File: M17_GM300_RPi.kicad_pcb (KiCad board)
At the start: 2 copper layers, 85 x 56 mm, 49 parts, among them J1 RJ45, J2 SJ1-3523N, J3 1935161, J4 DB9_Female, J5 RPi Header, Q1 2N7000, Q2 2N7000, Q3 2N7000, Q4 2N7000, U1 LM2576HVS-5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

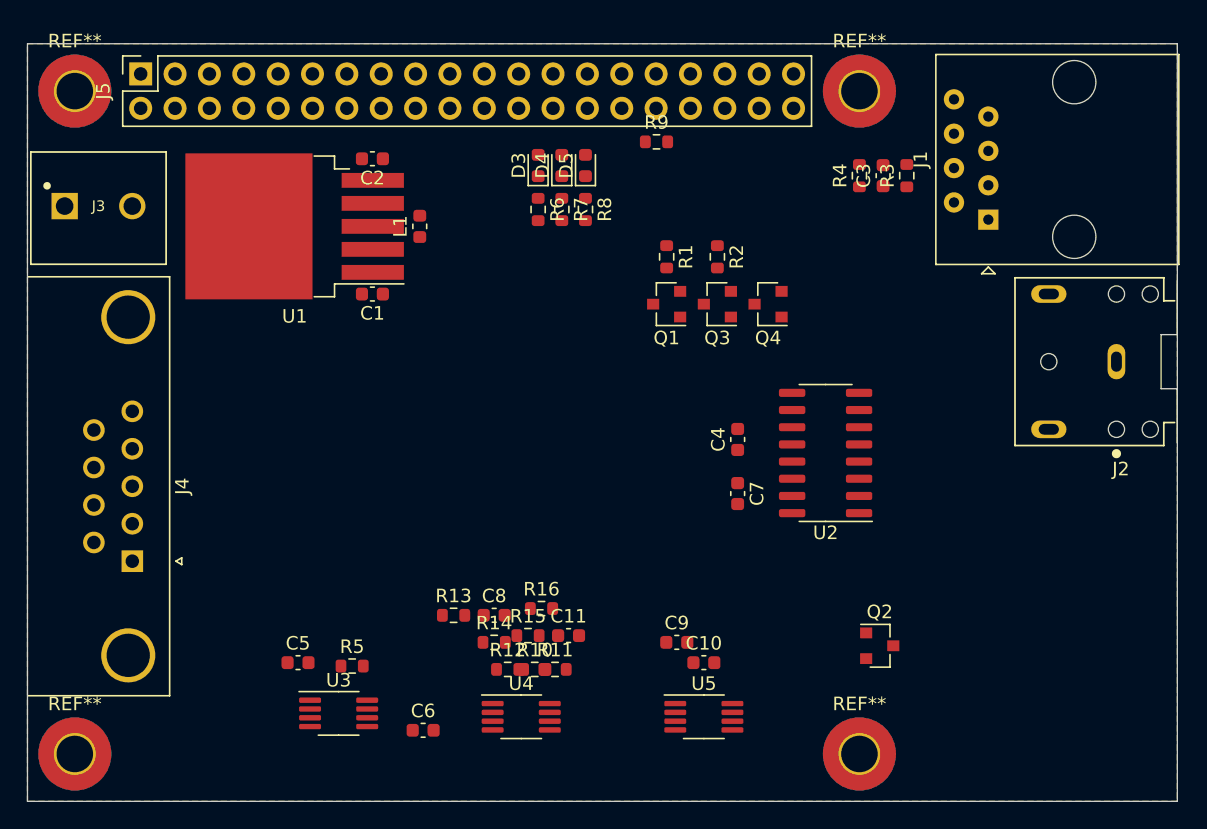
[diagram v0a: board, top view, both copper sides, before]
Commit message: pcb parts grouped by function
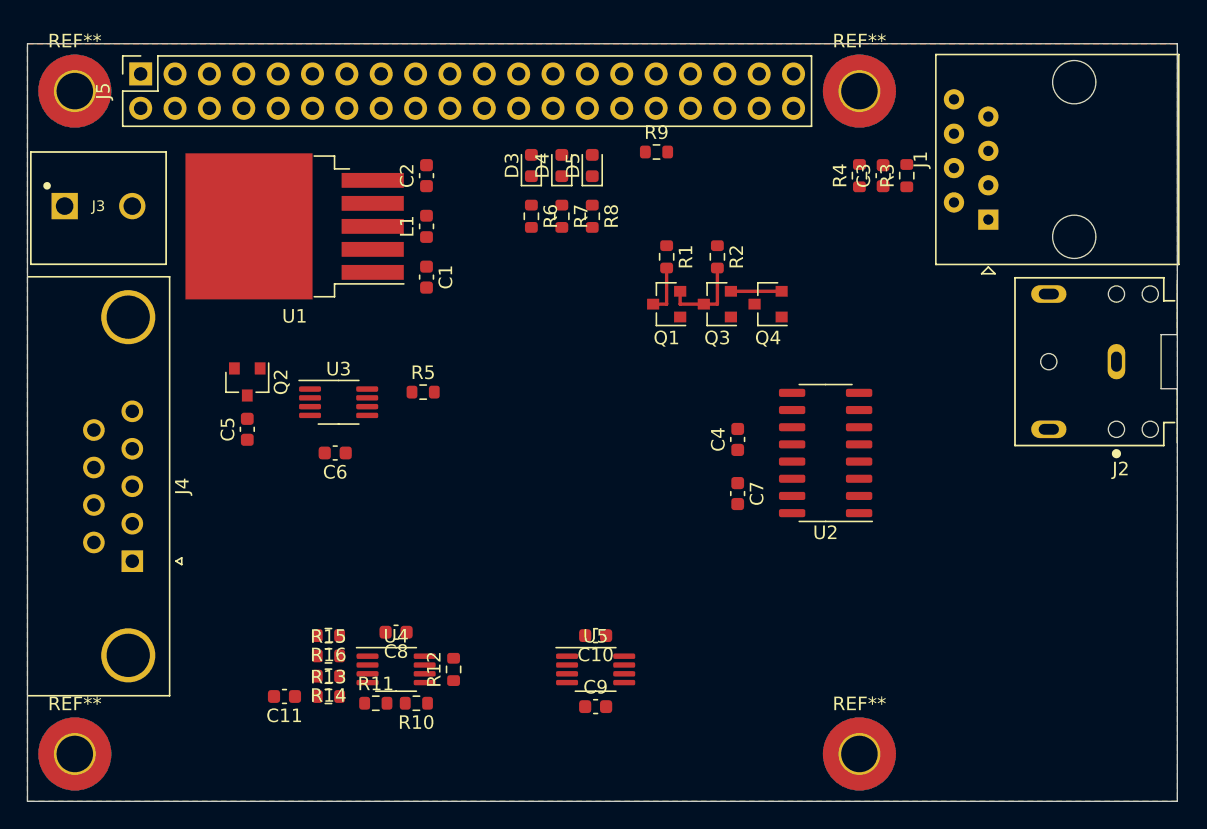
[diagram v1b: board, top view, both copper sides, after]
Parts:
- moved Q2 50.7 mm to (181.2, 75.0), turned to 270 degrees
- moved U3 23.0 mm to (188.0, 76.5)
- moved C6 21.5 mm to (187.8, 80.2), turned to 180 degrees
- moved C11 21.5 mm to (184.0, 98.2), turned to 180 degrees
- moved R5 20.9 mm to (194.2, 75.8)
- moved C5 17.7 mm to (181.2, 78.5), turned to 90 degrees
- moved R16 15.9 mm to (187.2, 93.8), turned to 180 degrees
- moved R15 14.8 mm to (187.2, 95.2)
- moved R11 13.5 mm to (190.8, 98.8)
- moved R14 12.5 mm to (187.2, 96.8), turned to 180 degrees
- moved R13 11.0 mm to (187.2, 98.2)
- moved U4 9.89 mm to (192.2, 96.2)
- moved R10 9.10 mm to (193.8, 98.8), turned to 180 degrees
- moved U5 8.73 mm to (207.0, 96.2)
- moved C10 8.25 mm to (207.0, 93.8), turned to 180 degrees
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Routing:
- net SW2: track 0.00 -> 6.38 mm
- net TX_EN: track 0.00 -> 3.75 mm
- net SW1: track 0.00 -> 3.67 mm

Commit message: Created new symbol and footprint for new power supply; removed old and added new power supply to schem; updated pcb with the changes.
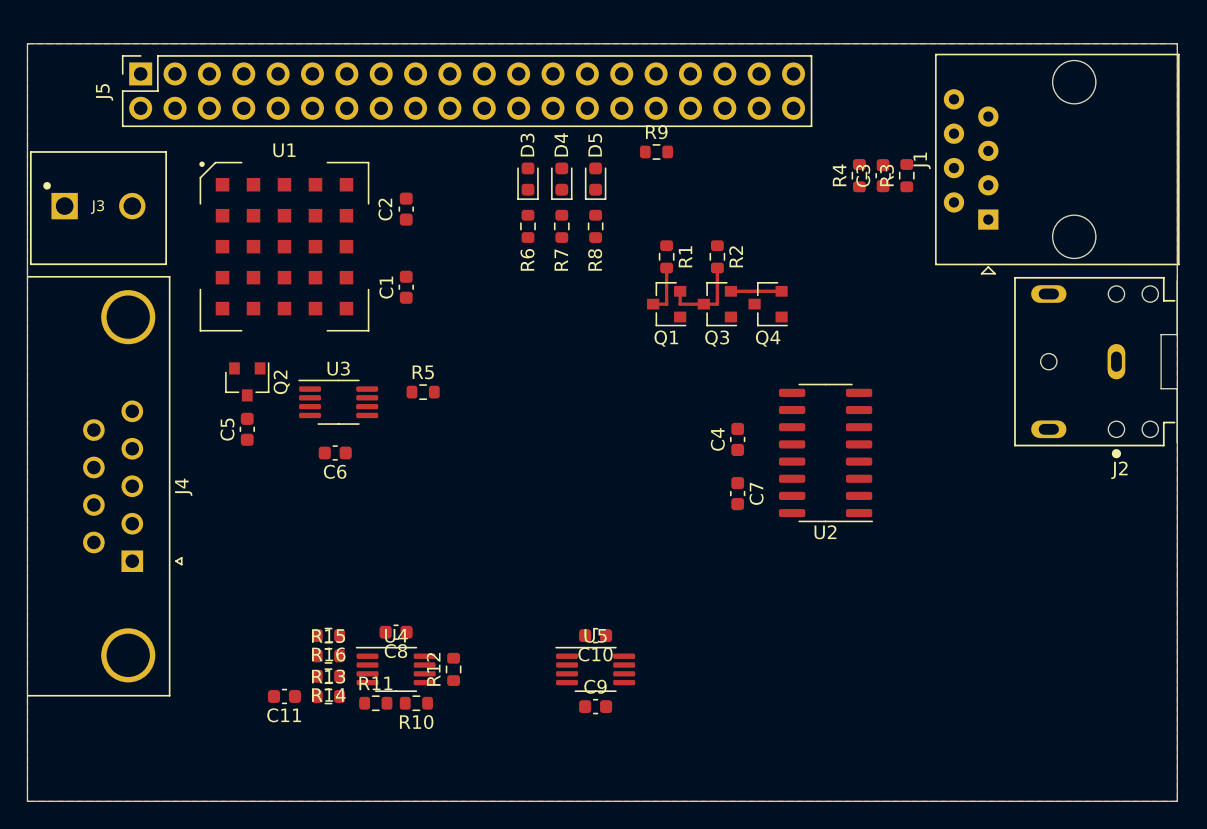
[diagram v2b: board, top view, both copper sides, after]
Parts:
- removed L1: 100 uH, Inductor_SMD:L_0603_1608Metric
- removed REF** (x4): MountingHole_2.7mm_M2.5_Pad_TopBottom, MountingHole:MountingHole_2.7mm_M2.5_Pad_TopBottom
- C1: value 100 uF -> 1000 uF
- U1: value LM2576HVS-5 -> RPM5.0-6.0; footprint Package_TO_SOT_SMD:TO-263-5_TabPin3 -> Power_Supplies:RPM5.0-6.0
- moved C2 2.89 mm to (193.0, 62.2), turned to 270 degrees
- moved C1 1.68 mm to (193.0, 68.0), turned to 90 degrees
- moved U1 1.68 mm to (184.0, 65.0), turned to 0 degrees
- moved D3 1.03 mm to (202.0, 60.0)
- moved D5 1.03 mm to (207.0, 60.0)
- moved D4 1.00 mm to (204.5, 60.0)
- moved R6 0.79 mm to (202.0, 63.5)
- moved R8 0.79 mm to (207.0, 63.5)
- moved R7 0.75 mm to (204.5, 63.5)

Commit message: increased passives to 0805. preliminary layout.
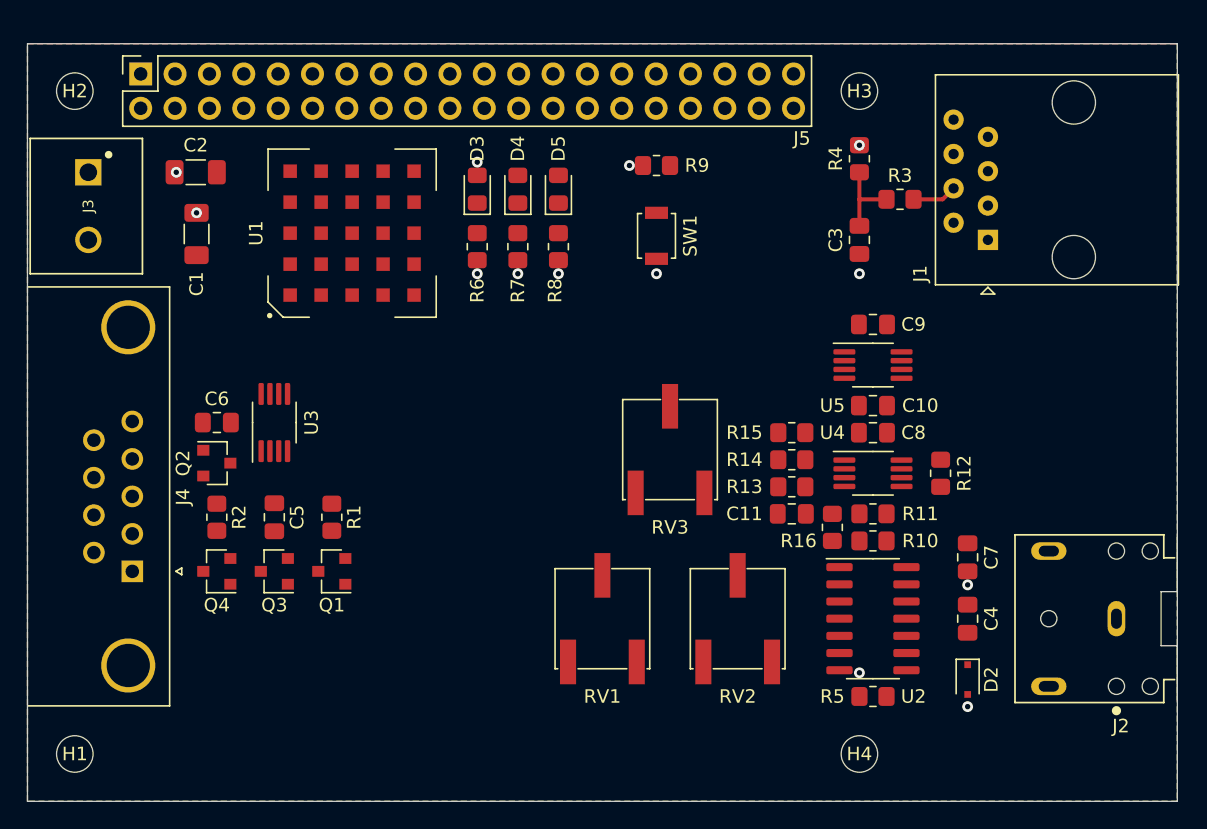
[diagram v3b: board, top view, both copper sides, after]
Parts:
- added D2: 2V7, Diode_SMD:D_SOD-323F, F.Cu at (234.5, 97.0)
- added H1: MountingHole, MountingHole:MountingHole_2.7mm_M2.5, F.Cu at (168.5, 102.5)
- added H2: MountingHole, MountingHole:MountingHole_2.7mm_M2.5, F.Cu at (168.5, 53.5)
- added H3: MountingHole, MountingHole:MountingHole_2.7mm_M2.5, F.Cu at (226.5, 53.5)
- added H4: MountingHole, MountingHole:MountingHole_2.7mm_M2.5, F.Cu at (226.5, 102.5)
- added RV1: 1K, Potentiometer_SMD:Potentiometer_Bourns_3361P_Vertical, F.Cu at (207.5, 92.5)
- added RV2: 4K7, Potentiometer_SMD:Potentiometer_Bourns_3361P_Vertical, F.Cu at (217.5, 92.5)
- added RV3: 4K7, Potentiometer_SMD:Potentiometer_Bourns_3361P_Vertical, F.Cu at (212.5, 80.0)
- added SW1: SW_Push, Button_Switch_SMD:SW_SPST_B3U-1000P, F.Cu at (211.5, 64.2)
- C1, C2: footprint Capacitor_SMD:C_0603_1608Metric -> Capacitor_SMD:C_1206_3216Metric_Pad1.33x1.80mm_HandSolder
- C10, C11, C3, C4, C5, C6, C7, C8, C9: footprint Capacitor_SMD:C_0603_1608Metric -> Capacitor_SMD:C_0805_2012Metric_Pad1.18x1.45mm_HandSolder
- D3, D4, D5: footprint LED_SMD:LED_0603_1608Metric -> LED_SMD:LED_0805_2012Metric_Pad1.15x1.40mm_HandSolder
- R1, R10, R11, R12, R13, R14, R15, R16, R2, R3, R4, R5, R6, R7, R8, R9: footprint Resistor_SMD:R_0603_1608Metric -> Resistor_SMD:R_0805_2012Metric_Pad1.20x1.40mm_HandSolder
- U2: footprint Package_SO:SOIC-16_3.9x9.9mm_P1.27mm -> Package_SO:SOIC-14_3.9x8.7mm_P1.27mm
- moved Q4 45.3 mm to (179.0, 89.0)
- moved R2 41.7 mm to (179.0, 85.0)
- moved R5 40.1 mm to (227.5, 98.2)
- moved C11 39.9 mm to (221.5, 84.8)
- moved R11 39.3 mm to (227.5, 84.8)
- moved R12 38.8 mm to (232.5, 81.8)
- moved Q3 38.2 mm to (183.2, 89.0)
- moved C8 38.2 mm to (227.5, 78.8)
- moved U4 38.1 mm to (227.5, 81.8)
- moved R16 38.1 mm to (224.5, 85.8), turned to 270 degrees
- moved R15 38.0 mm to (221.5, 78.8)
- moved R14 37.8 mm to (221.5, 80.8)
- moved R13 37.6 mm to (221.5, 82.8)
- moved R10 35.8 mm to (227.5, 86.8), turned to 0 degrees
- moved C9 34.9 mm to (227.5, 70.8), turned to 180 degrees
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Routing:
- net SW2: track 6.38 -> 0.00 mm
- net Net-(C3-Pad1): track 0.00 -> 5.96 mm
- net TX_EN: track 3.75 -> 0.00 mm
- net SW1: track 3.67 -> 0.00 mm
- net MIC: track 0.00 -> 3.30 mm
- net GND: vias 0 -> 10
- net +BATT: vias 0 -> 1
- net +5V: vias 0 -> 1
- net +3V3: vias 0 -> 1
- added copper zone on PWR, net +3V3
- added copper zone on B.Cu, net GND
- added copper zone on GND, net GND
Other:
- copper layers 2 -> 4

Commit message: updated layout to proposed final
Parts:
- U3: footprint Package_SO:MSOP-8_3x3mm_P0.65mm -> Package_SO:SOIC-8_3.9x4.9mm_P1.27mm
- moved C6 30.6 mm to (209.0, 84.0), turned to 90 degrees
- moved R5 30.1 mm to (201.0, 84.0), turned to 270 degrees
- moved U3 24.8 mm to (205.0, 90.0), turned to 0 degrees
- moved C5 21.8 mm to (205.0, 84.0)
- moved RV3 20.3 mm to (216.0, 100.0)
- moved C9 17.0 mm to (241.0, 81.0)
- moved RV1 15.4 mm to (194.0, 100.0)
- moved RV2 14.6 mm to (205.0, 100.0)
- moved C10 14.0 mm to (241.0, 73.0)
- moved C11 13.9 mm to (229.0, 73.0), turned to 0 degrees
- moved U5 13.9 mm to (241.0, 77.0)
- moved R11 10.8 mm to (235.0, 77.0)
- moved R13 9.86 mm to (223.0, 73.0)
- moved R10 9.45 mm to (235.0, 81.0), turned to 180 degrees
- moved R1 9.18 mm to (183.0, 77.0)
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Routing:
- net Net-(C4-Pad1): track 0.00 -> 11.4 mm
- net Net-(C3-Pad1): track 5.96 -> 0.00 mm, vias 0 -> 1
- net MIC: track 3.30 -> 0.00 mm
- net GND: vias 10 -> 9
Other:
- board text added: "GM300 to RPi Interface Board"
- board text added: "RX Gain"
- board text added: "RX Vol"
- board text added: "TX Dev"
- board text added: "prototype"

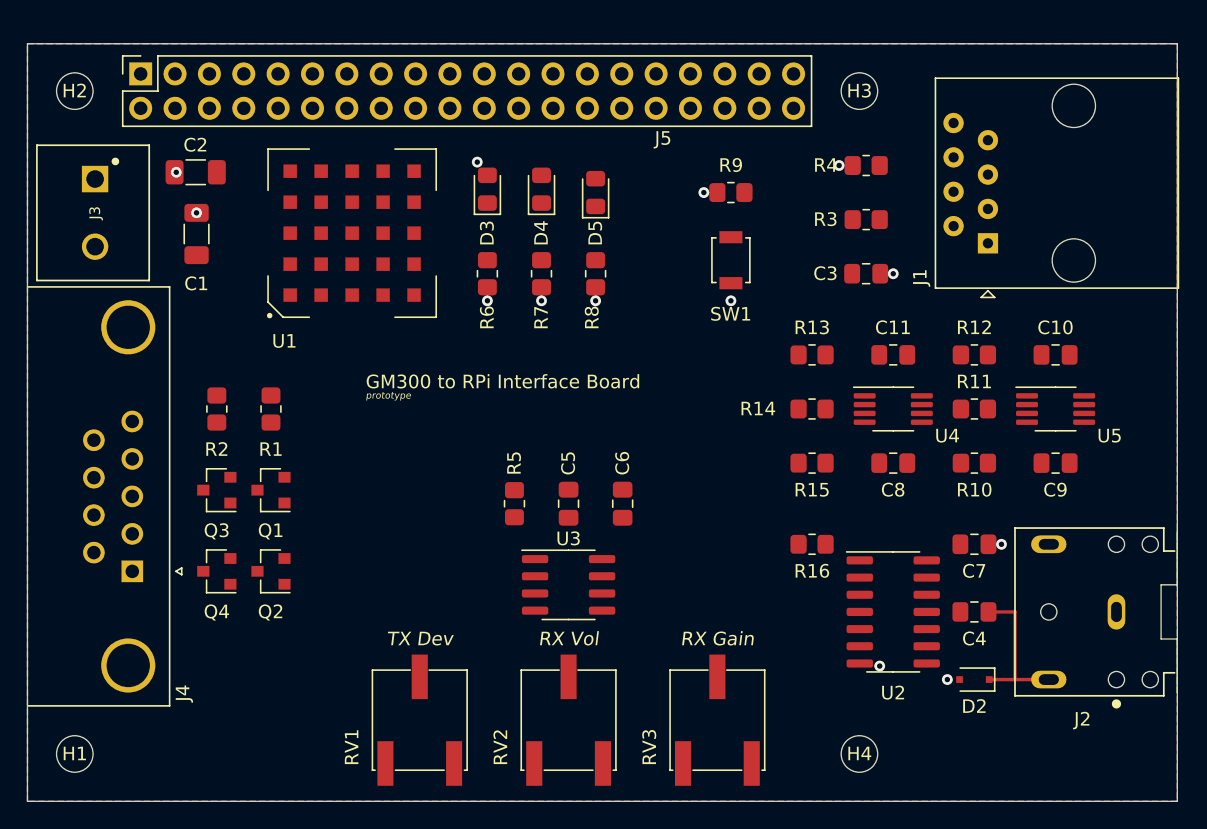
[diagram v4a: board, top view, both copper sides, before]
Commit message: part and footprint updates, routing
updated parts and footprints for header and transistors. updated layout. most routing is complete pending changes to schematic.
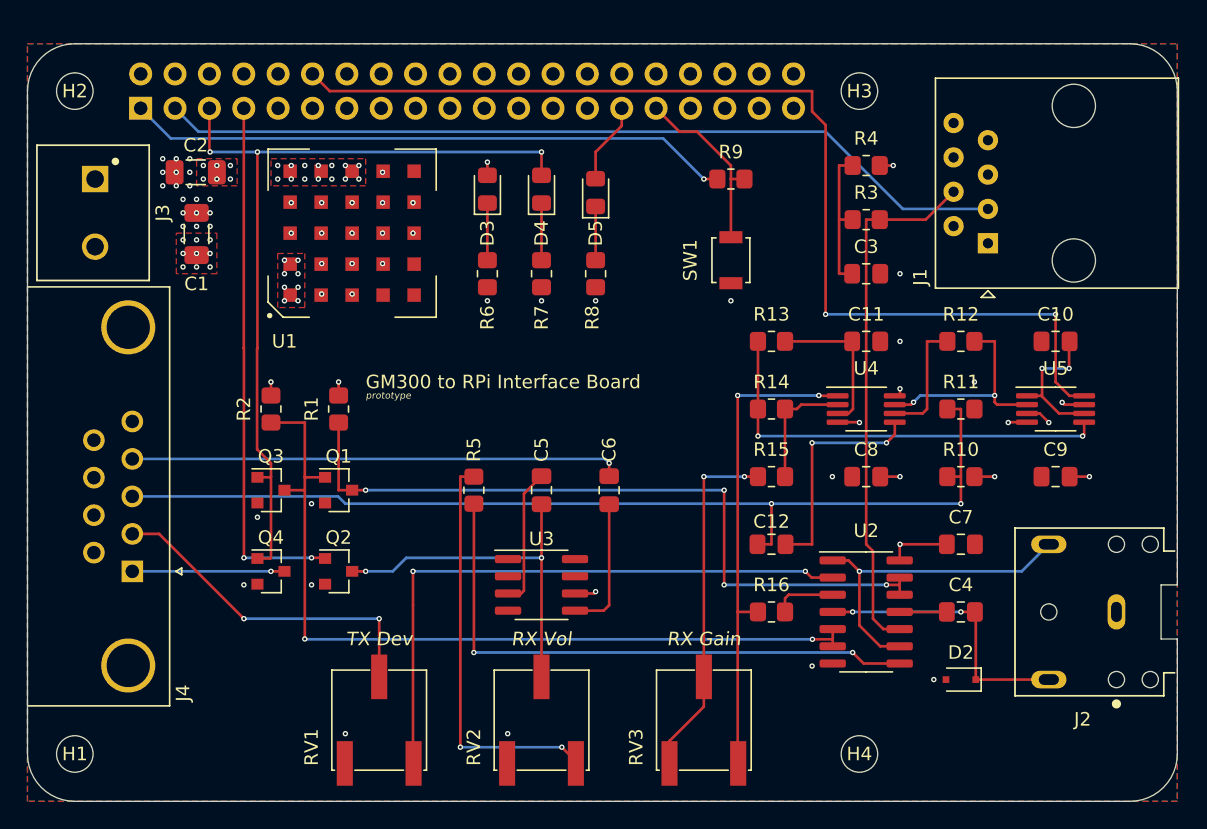
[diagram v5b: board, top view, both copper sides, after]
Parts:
- added C12: 2.2uF, Capacitor_SMD:C_0805_2012Metric_Pad1.18x1.45mm_HandSolder, F.Cu at (220.0, 87.0)
- J5: moved to B.Cu
- Q1, Q2, Q3, Q4: value 2N7000 -> BSS138
- moved R16 5.83 mm to (220.0, 92.0)
- moved Q1 5.00 mm to (188.0, 83.0), turned to 0 degrees
- moved Q2 5.00 mm to (188.0, 89.0), turned to 0 degrees
- moved R1 5.00 mm to (188.0, 77.0)
- moved Q3 4.00 mm to (183.0, 83.0), turned to 0 degrees
- moved Q4 4.00 mm to (183.0, 89.0), turned to 0 degrees
- moved R2 4.00 mm to (183.0, 77.0)
- moved R13 3.16 mm to (220.0, 72.0)
- moved R15 3.16 mm to (220.0, 82.0)
- moved R5 3.16 mm to (198.0, 83.0)
- moved R14 3.00 mm to (220.0, 77.0)
- moved RV1 3.00 mm to (191.0, 100.0)
- moved J5 2.54 mm to (173.4, 54.8), turned to 270 degrees
- moved C11 2.24 mm to (227.0, 72.0)
- moved C5 2.24 mm to (203.0, 83.0)
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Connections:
- Q1 pad 1: GND -> SW2
- Q1 pad 2: SW2 -> GND
- Q2 pad 1: GND -> MUTE
- Q2 pad 2: MUTE -> GND
- Q3 pad 1: GND -> TX_EN
- Q3 pad 2: TX_EN -> GND
- Q4 pad 1: GND -> TX_EN
- Q4 pad 2: TX_EN -> GND
- RV3 pad 1: Net-(R16-Pad1) -> Net-(R15-Pad1)
- RV3 pad 3: Net-(R15-Pad1) -> Net-(R16-Pad1)
- U4 pad 5: RX_AUD -> Net-(C12-Pad2)
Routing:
- net FLT_CLK: track 0.00 -> 78.9 mm, vias 0 -> 2
- net RX_AUD: track 0.00 -> 74.5 mm, vias 0 -> 2
- net PTT: track 0.00 -> 63.2 mm
- net TX_EN: track 0.00 -> 62.0 mm, vias 0 -> 3
- net SW2: track 0.00 -> 61.8 mm, vias 0 -> 2
- net SW1: track 0.00 -> 54.8 mm, vias 0 -> 4
- net +3V3: track 0.00 -> 53.2 mm, vias 1 -> 7
- net MOD_OUT: track 0.00 -> 45.4 mm, vias 0 -> 2
- net SPK_AMP: track 0.00 -> 42.8 mm, vias 0 -> 2
- net MIC: track 0.00 -> 39.3 mm
- net MUTE: track 0.00 -> 39.3 mm, vias 0 -> 2
- net SPK_OUT: track 0.00 -> 36.3 mm, vias 0 -> 1
- net Net-(R16-Pad1): track 0.00 -> 36.1 mm, vias 0 -> 2
- net Net-(R13-Pad1): track 0.00 -> 32.1 mm, vias 0 -> 2
- net Net-(R5-Pad1): track 0.00 -> 30.1 mm, vias 0 -> 2
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- added copper zone on F.Cu, net +5V
- added copper zone on PWR, net +5V
- added copper zone on F.Cu, net +BATT
- added copper zone on PWR, net +BATT
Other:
- outline, holes or cut-outs redrawn
- net class Default: clearance 0.2 -> 0.1; trace_width 0.25 -> 0.1; via_dia 0.8 -> 0.4; via_drill 0.4 -> 0.2
- rule trace_clearance: 0.2 -> 0.1
- rule trace_min: 0.2 -> 0.1
- rule via_min_drill: 0.3 -> 0.2
